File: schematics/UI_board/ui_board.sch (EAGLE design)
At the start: 116 parts, among them IC10 74HCT32N, IC11 74HCT14N, IC12 74HCT14N, IC13 74HCT393N, IC2 74HCT151N, IC3 74HCT32N, IC4 74HCT74N, IC5 74HCT08N, IC6 74HCT32N, IC7 74HCT14N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

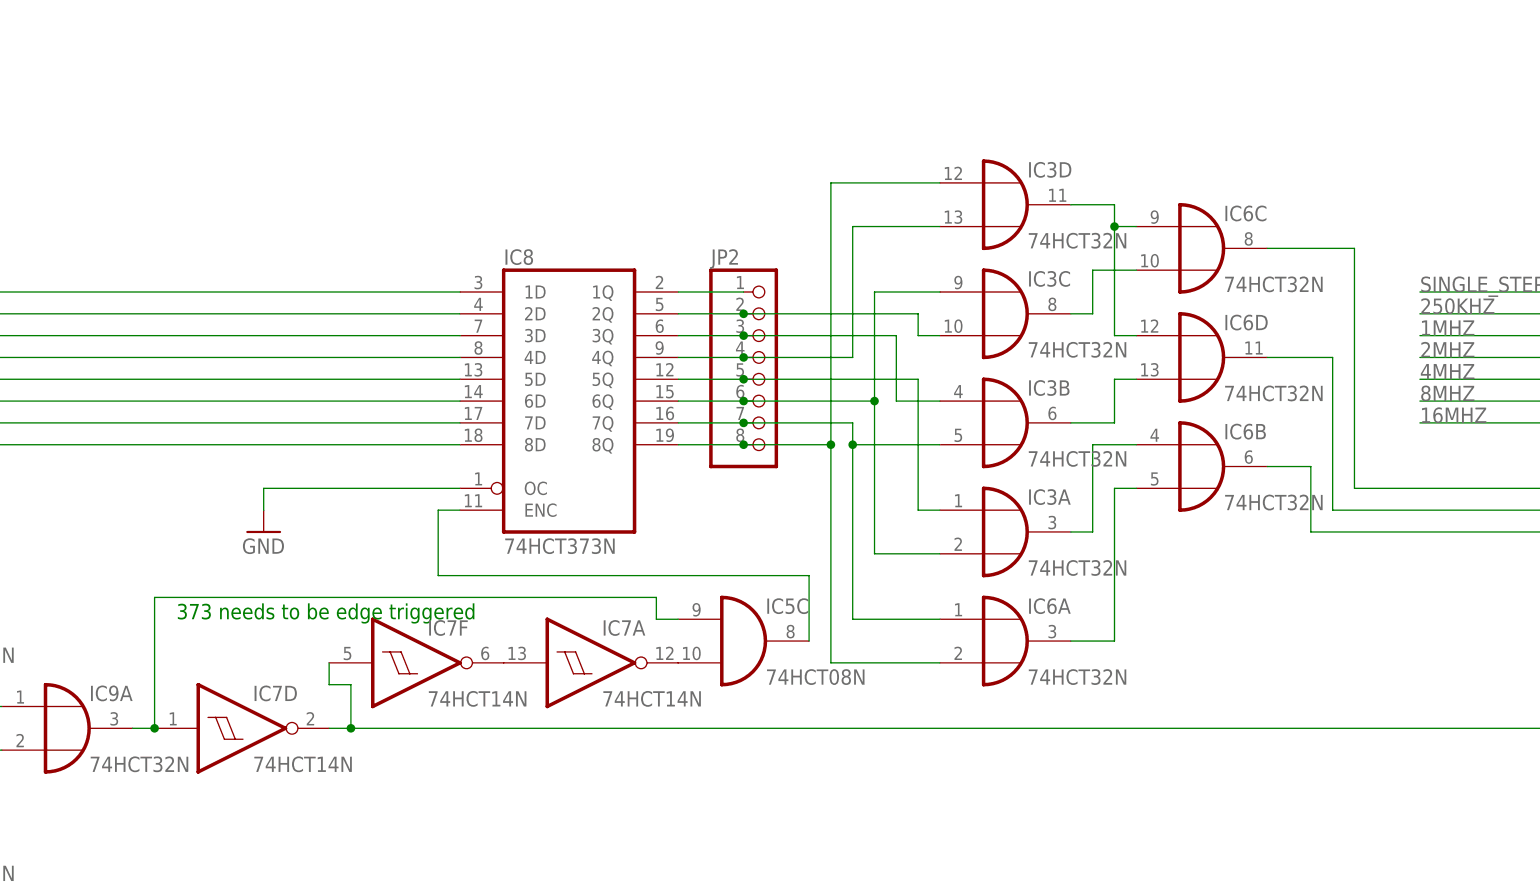
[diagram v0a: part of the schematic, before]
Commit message: fix latex docs
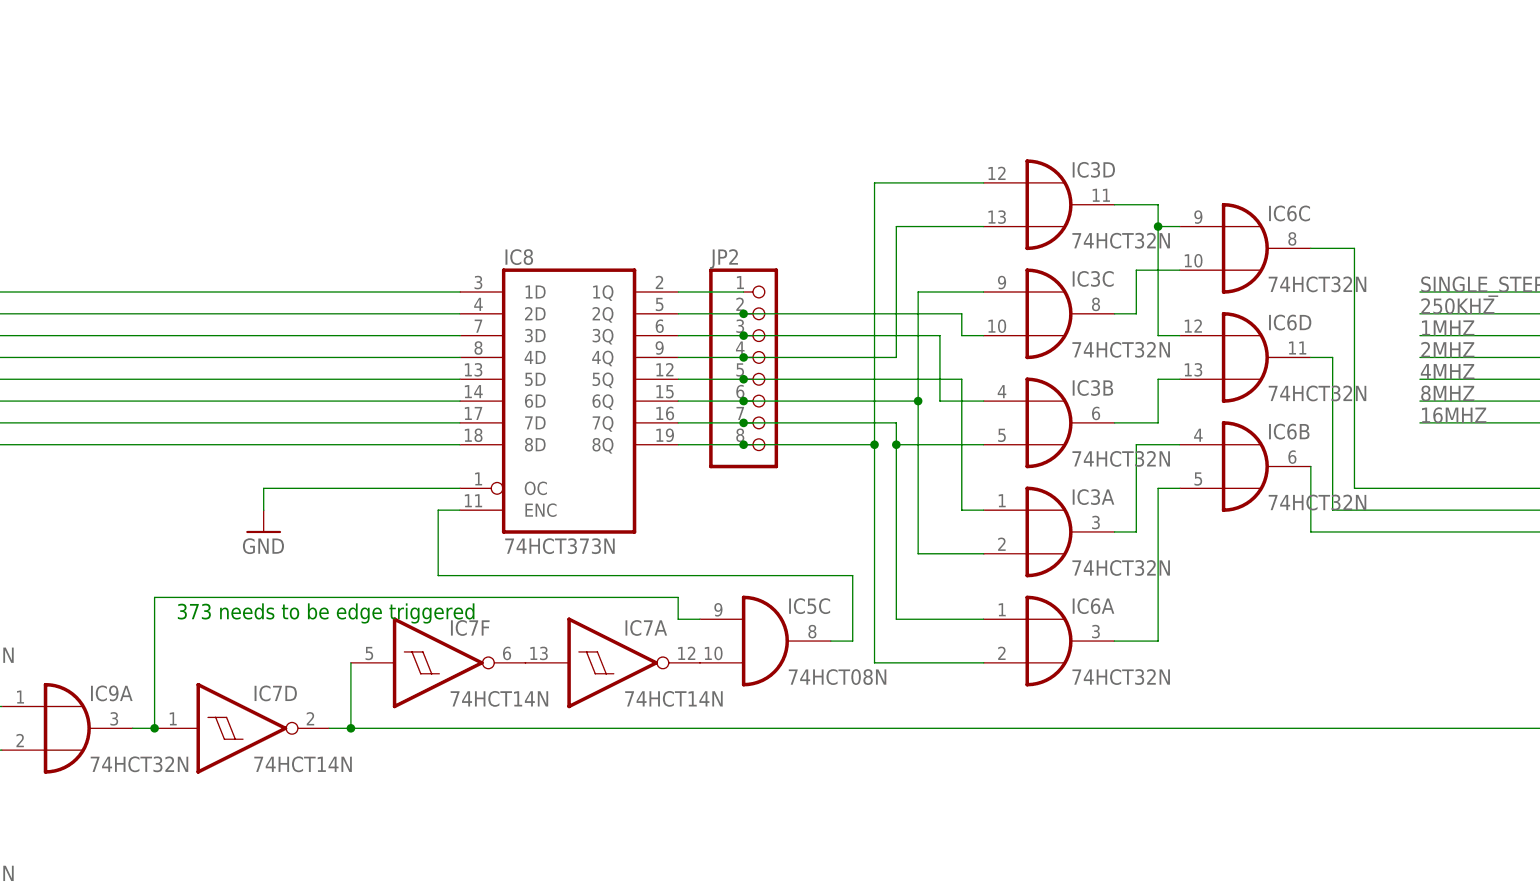
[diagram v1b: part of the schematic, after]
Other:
- moved on the sheet: IC3A, IC3B, IC3C, IC3D, IC5C, IC6A, IC6B, IC6C, IC6D, IC7A, IC7F

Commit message: feature freeze. I will now solder the Control Unit
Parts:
- removed LED7: (no value), led:LED3MM
- removed R35: 22k, rcl:R-EU_R1206
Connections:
- removed net CYCL_7: JP1.34, LED7.A
- removed net N$66: LED7.C, R35.2
- net CYCL_1: now also JP1.26; no longer JP1.22
- net CYCL_2: now also JP1.28; no longer JP1.24
- net CYCL_3: now also JP1.30; no longer JP1.26
- net CYCL_4: now also JP1.32; no longer JP1.28
- net CYCL_5: now also JP1.34; no longer JP1.30
- net CYCL_6: now also JP1.36; no longer JP1.32
- net GND: now also JP1.22, JP1.24; no longer JP1.36, R35.1
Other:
- moved on the sheet: LED1, LED2, LED3, LED4, LED5, LED6, R29, R30, R31, R32, R33, R34
